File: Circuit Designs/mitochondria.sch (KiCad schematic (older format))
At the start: 59 parts

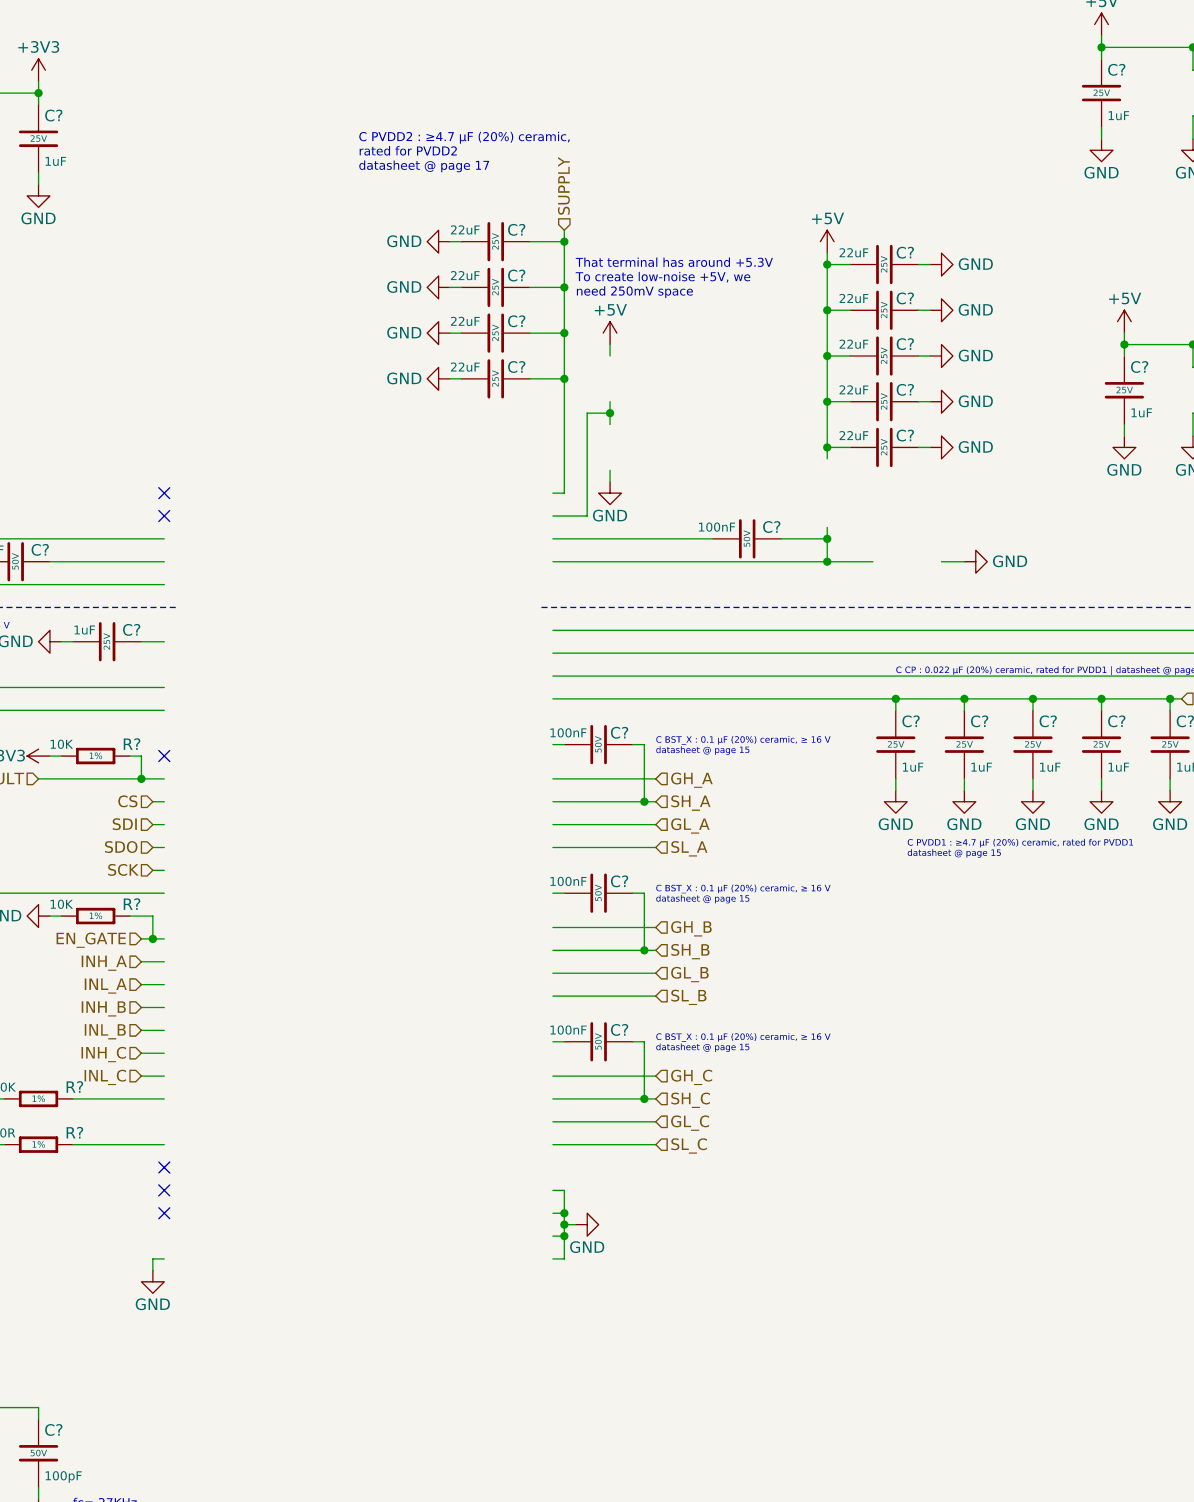
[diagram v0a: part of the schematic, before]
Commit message: added buck converter's components
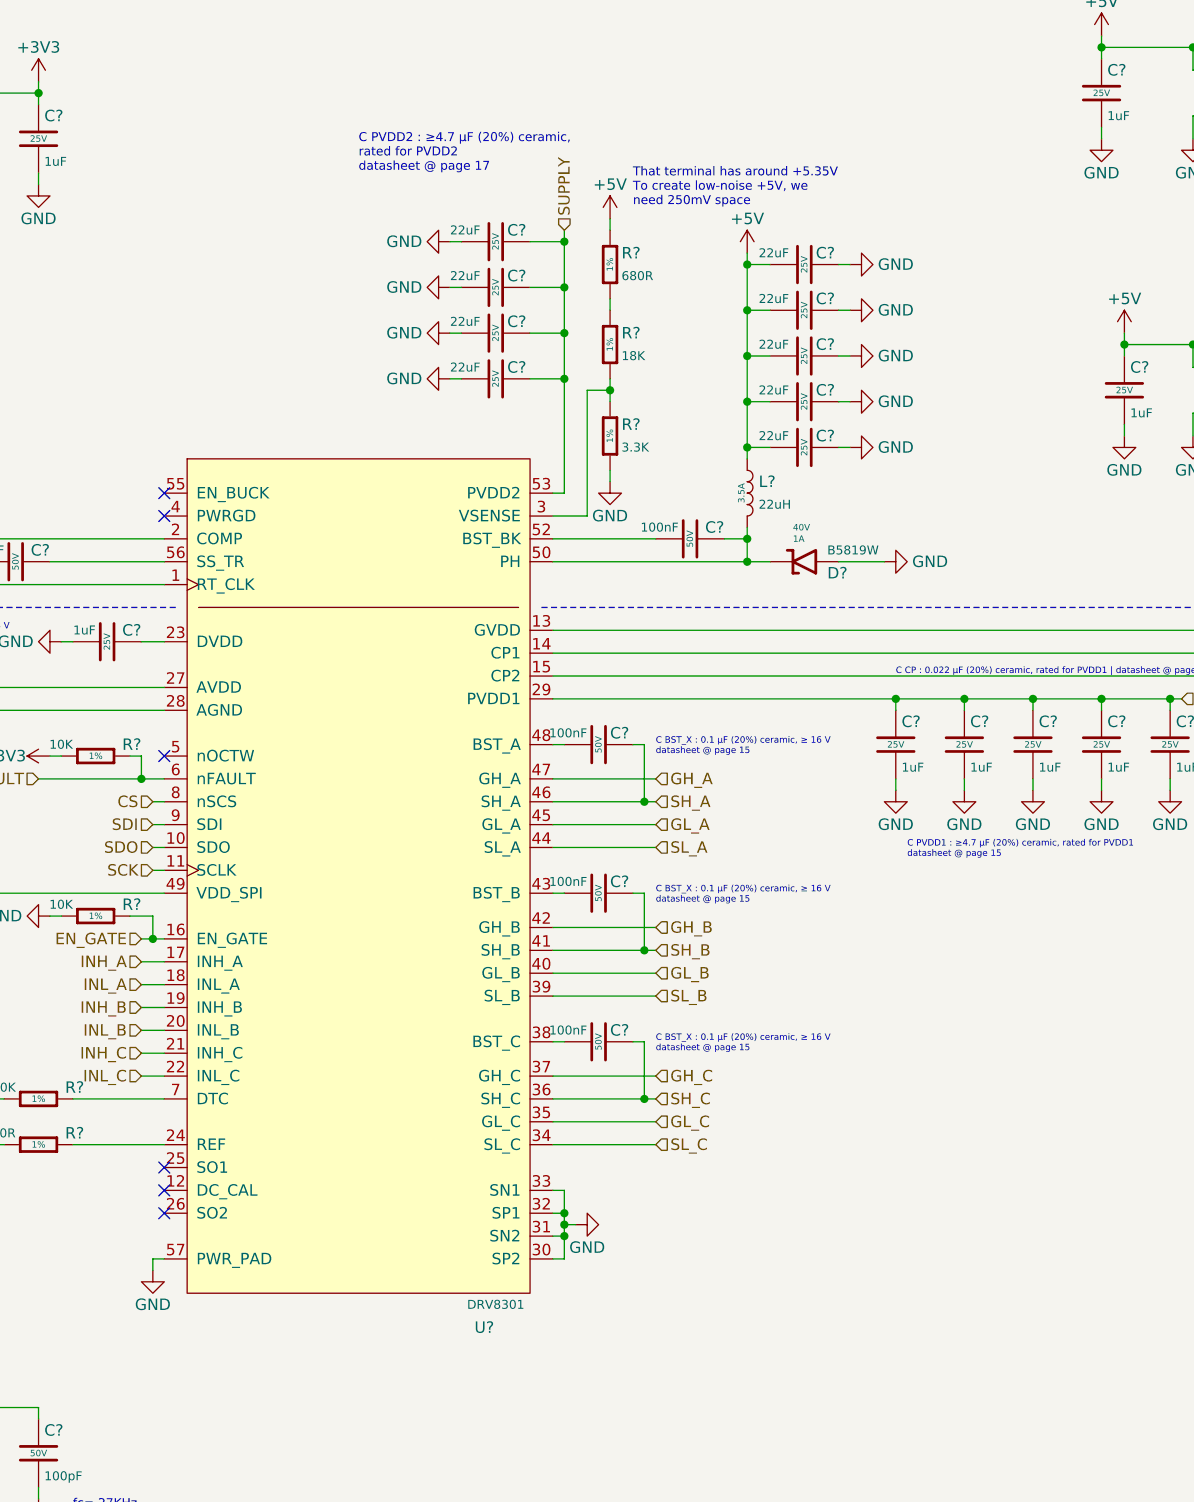
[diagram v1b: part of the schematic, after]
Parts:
- added D?: B5819W, Diode_SMD:D_SOD-123, symbol CoE_Diode:B5819W
- added L?: 22uH, Inductor_SMD:L_Taiyo-Yuden_NR-60xx, symbol CoE_Inductor:22uH
- added R?: 3.3K, Resistor_SMD:R_0402_1005Metric, symbol CoE_Resistor:3.3K
- added R?: 18K, Resistor_SMD:R_0402_1005Metric, symbol CoE_Resistor:18K
- added R?: 680R, Resistor_SMD:R_0402_1005Metric, symbol CoE_Resistor:680R
- added U?: DRV8301, Package_SO:HTSSOP-56-1EP_6.1x14mm_P0.5mm_EP3.61x6.35mm, symbol CoE_IntegratedCircuit:DRV8301
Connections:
- wire segments 268 -> 269
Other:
- note added: "That terminal has around +5.35V\nTo create low-noise +5V, we \nneed 250mV space"
- note removed: "That terminal has around +5.3V\nTo create low-noise +5V, we \nneed 250mV space"
- moved on the sheet: C?

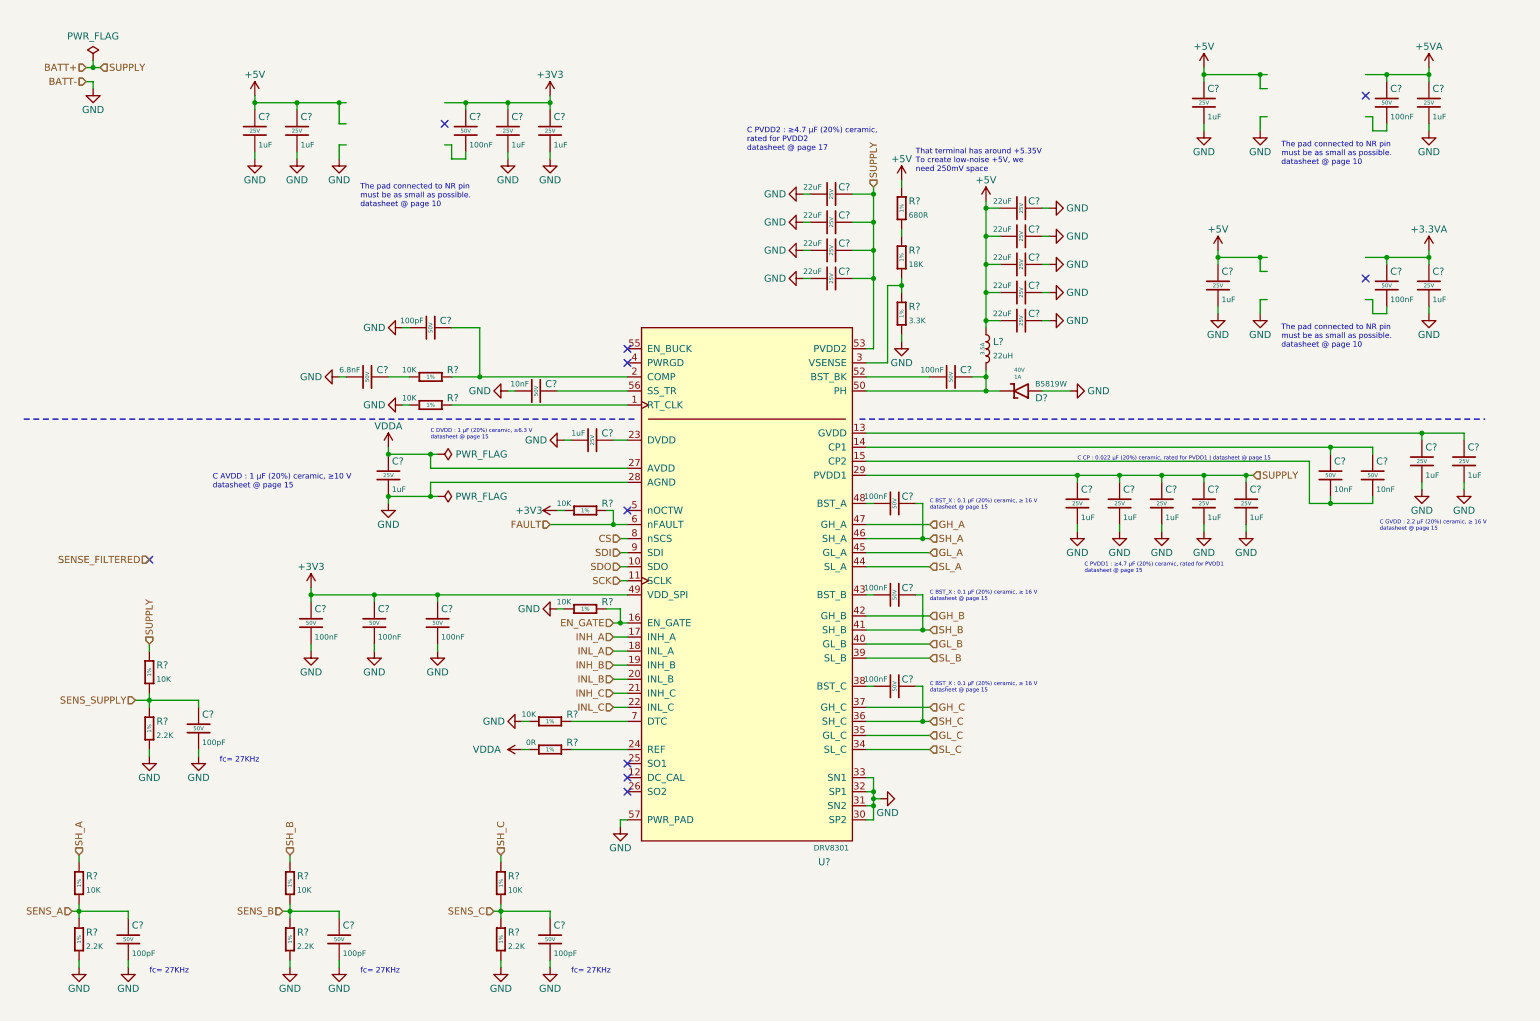
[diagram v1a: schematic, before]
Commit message: added motor driver and adjustable regulators. Now, it is the time to start the detailed review
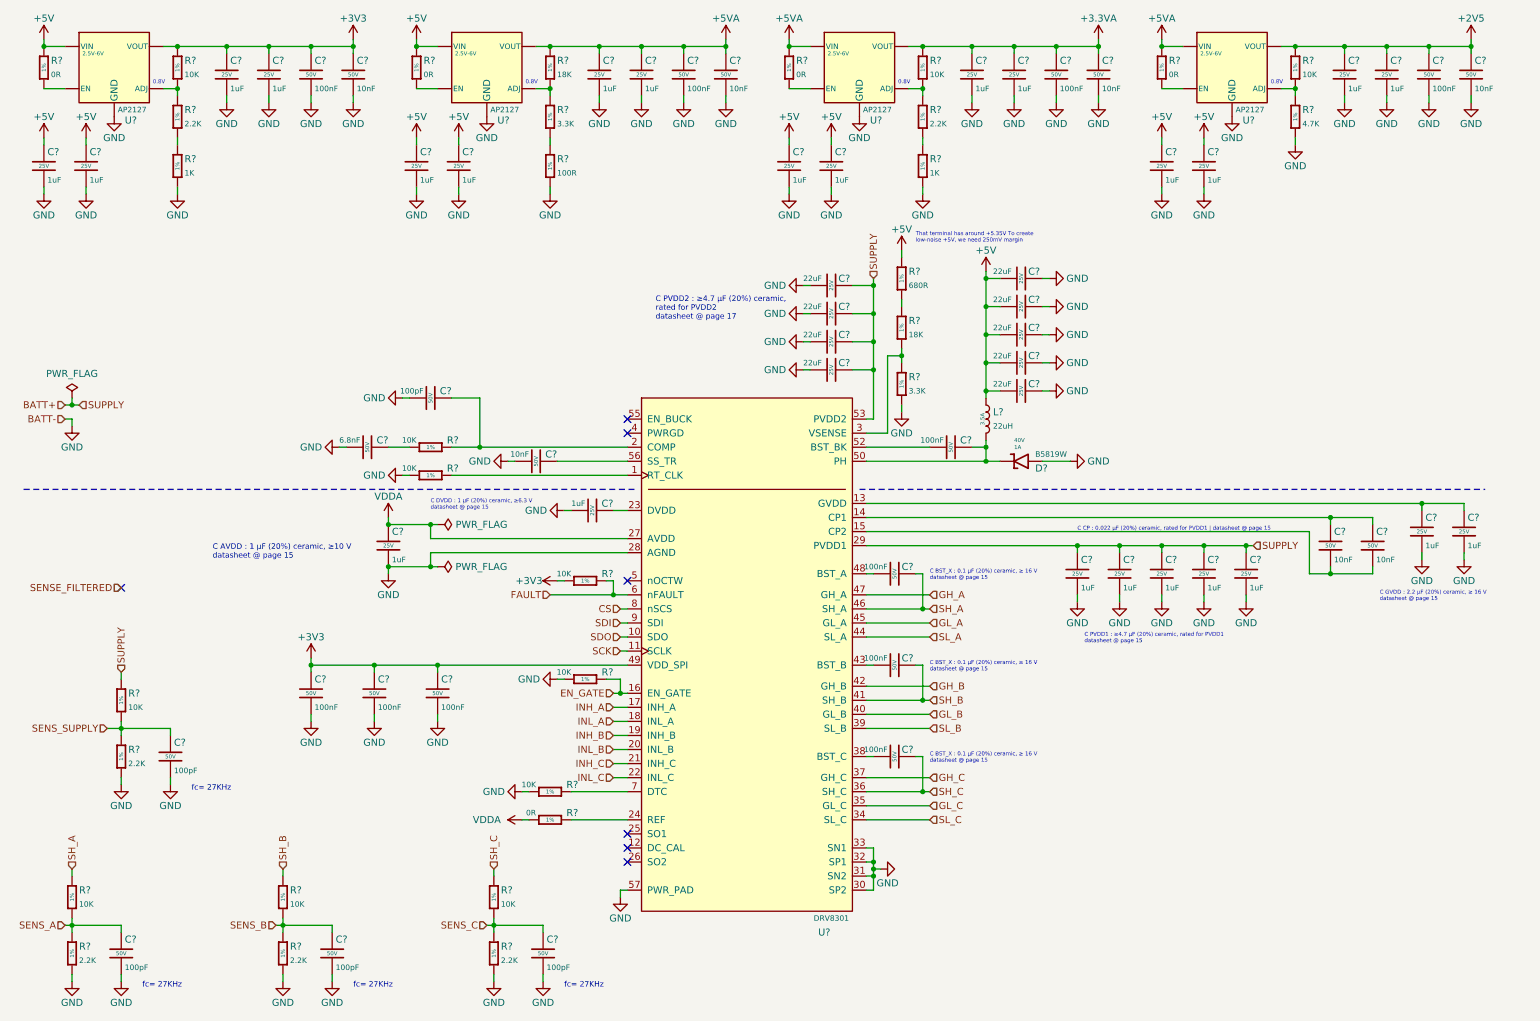
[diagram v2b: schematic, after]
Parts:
- removed C? (x6): 1uF, Capacitor_SMD:C_0402_1005Metric, symbol CoE_Capacitor:1uF
- removed C? (x3): 100nF, Capacitor_SMD:C_0402_1005Metric, symbol CoE_Capacitor:100nF
- added C? (x14): 1uF, Capacitor_SMD:C_0402_1005Metric, symbol CoE_Capacitor:1uF
- added C? (x4): 100nF, Capacitor_SMD:C_0402_1005Metric, symbol CoE_Capacitor:100nF
- added C? (x4): 10nF, Capacitor_SMD:C_0402_1005Metric, symbol CoE_Capacitor:10nF
- added R? (x4): 0R, Resistor_SMD:R_0402_1005Metric, symbol CoE_Resistor:0R
- added R? (x3): 10K, Resistor_SMD:R_0402_1005Metric, symbol CoE_Resistor:10K
- added R? (x2): 2.2K, Resistor_SMD:R_0402_1005Metric, symbol CoE_Resistor:2.2K
- added R? (x2): 1K, Resistor_SMD:R_0402_1005Metric, symbol CoE_Resistor:1K
- added R?: 18K, Resistor_SMD:R_0402_1005Metric, symbol CoE_Resistor:18K
- added R?: 3.3K, Resistor_SMD:R_0402_1005Metric, symbol CoE_Resistor:3.3K
- added R?: 100R, Resistor_SMD:R_0402_1005Metric, symbol CoE_Resistor:100R
- added R?: 4.7K, Resistor_SMD:R_0402_1005Metric, symbol CoE_Resistor:4.7K
- added U? (x4): AP2127, Package_TO_SOT_SMD:SOT-23-5, symbol CoE_IntegratedCircuit:AP2127
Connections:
- net labels added: +2V5
- wire segments 269 -> 305
- no-connect marks 10 -> 7
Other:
- note added: "0.8V"
- note added: "That terminal has around +5.35V To create \nlow-noise +5V, we need 250mV margin"
- note removed: "That terminal has around +5.35V\nTo create low-noise +5V, we \nneed 250mV space"
- note removed: "The pad connected to NR pin \nmust be as small as possible.\ndatasheet @ page 10"
- moved on the sheet: C?, D?, L?, R?, U?

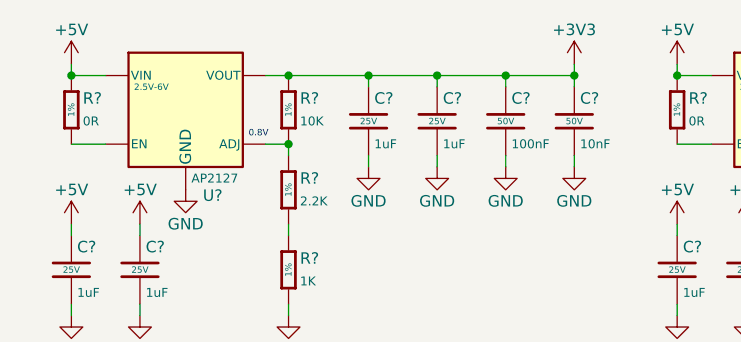
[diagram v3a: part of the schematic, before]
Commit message: edited myofibril file, added a related image about myofibrils
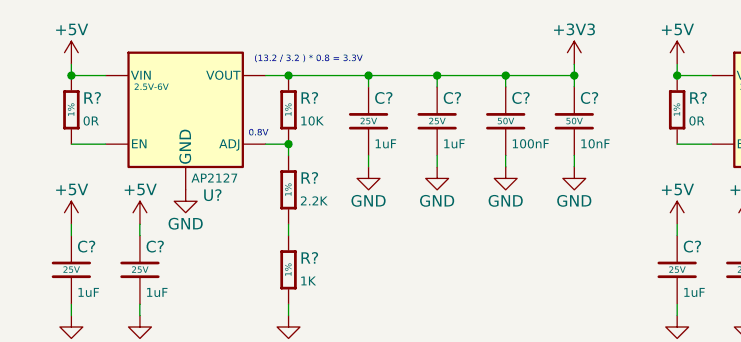
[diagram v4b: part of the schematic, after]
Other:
- note added: "(13.2 / 3.2 ) * 0.8 = 3.3V"
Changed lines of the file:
@@
 	9650 1200 9650 1150
 Connection ~ 9650 1150
+Text Notes 1550 800  0    28   ~ 0
+(13.2 / 3.2 ) * 0.8 = 3.3V
 $EndSCHEMATC
